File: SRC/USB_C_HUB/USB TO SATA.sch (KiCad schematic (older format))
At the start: 48 parts, among them J7 Bus_M.2_Socket_M, U9 TUSB9261, Y5 40MHz

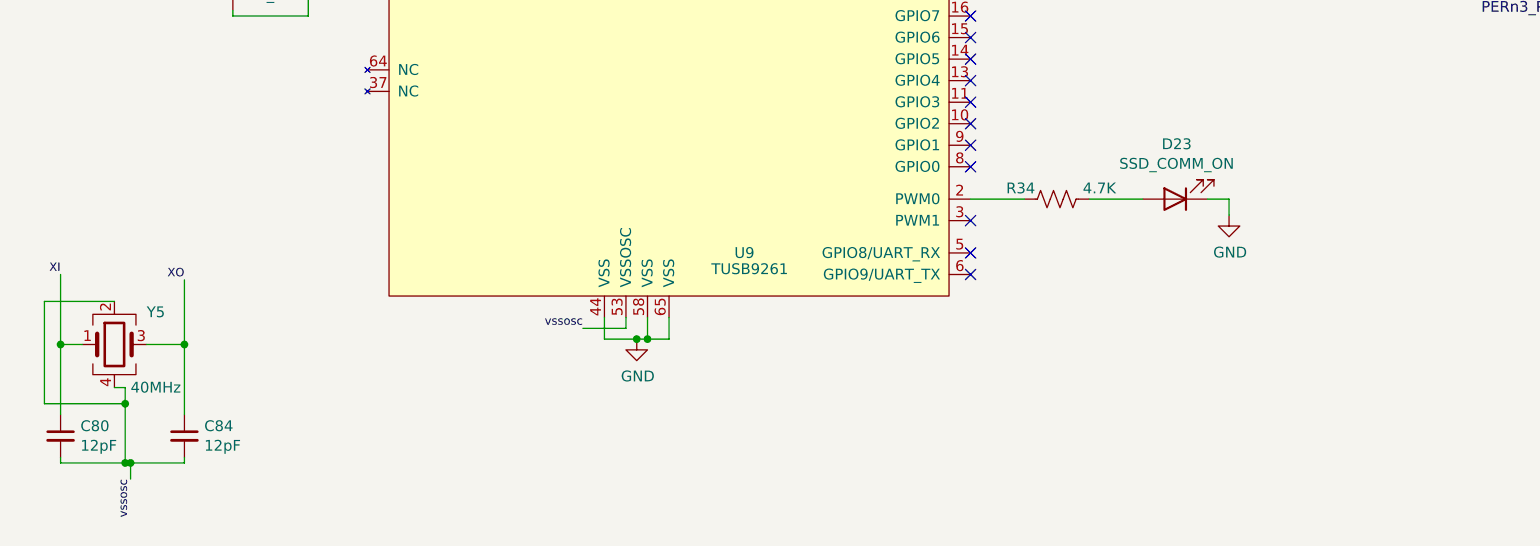
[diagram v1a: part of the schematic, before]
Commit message: schematic capture and footprint assignment complete. Pending approval
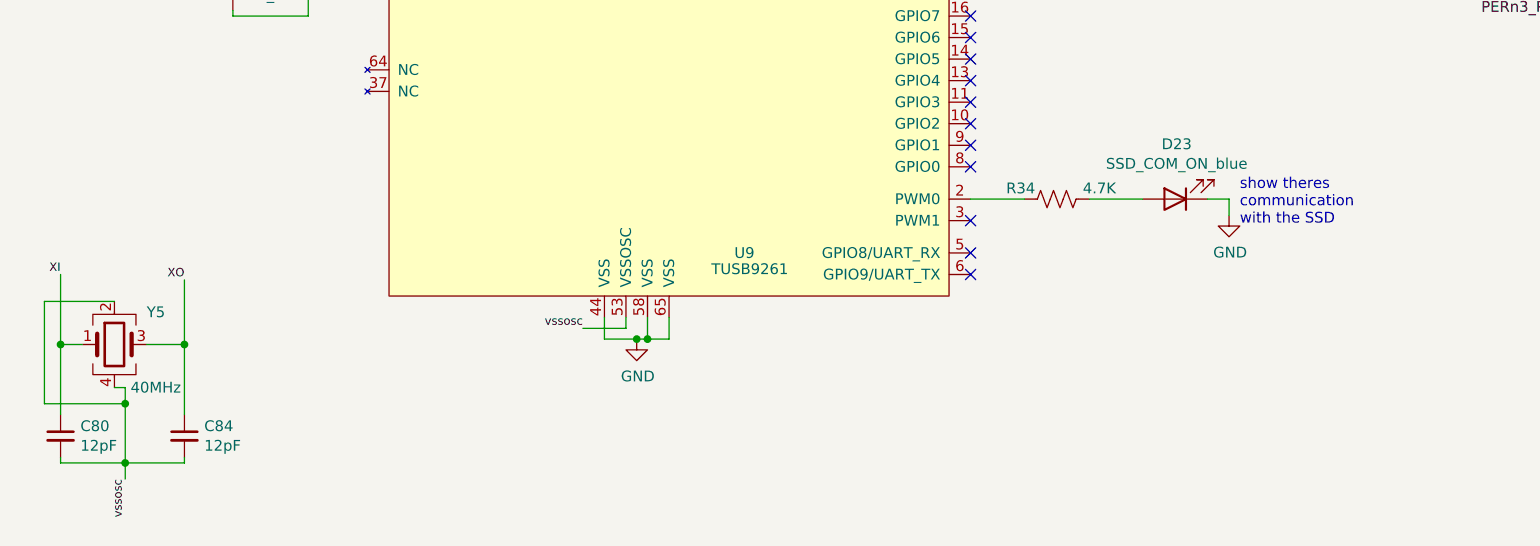
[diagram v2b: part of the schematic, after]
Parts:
- C100, C81: footprint (none) -> Capacitor_SMD:C_0402_1005Metric; Mfr No. (none) -> CL05A105KQ5NNNC
- C101: footprint (none) -> Capacitor_SMD:C_0402_1005Metric; Mfr No. (none) -> GRM155R60J226ME11D
- C102, C103, C104, C105, C106, C107, C108, C109, C110, C111, C112, C113, C114, C82, C83, C85, C86, C87, C88, C89, C90, C91, C92, C93, C94, C95, C96, C97, C98, C99: footprint (none) -> Capacitor_SMD:C_0402_1005Metric
- C79: footprint (none) -> Capacitor_SMD:C_0402_1005Metric; Mfr No. (none) -> C0402C103J5RECAUTO
- C80, C84: footprint (none) -> Capacitor_SMD:C_0402_1005Metric; Mfr No. (none) -> 0402CG120J500NT
- D23: value SSD_COMM_ON -> SSD_COM_ON_blue; footprint (none) -> LED_SMD:LED_0603_1608Metric; Field4 (none) -> 19-217/BHC-ZL1M2RY/3T
- J7: footprint (none) -> footprints:TE_1-2199119-3
- R101, R30, R31, R32, R33, R34, R35: footprint (none) -> Resistor_SMD:R_0402_1005Metric
- R29: footprint (none) -> Resistor_SMD:R_0402_1005Metric; Mfr No. (none) -> 0402WGF9092TCE
- U9: footprint (none) -> footprints:QFP40P900X900X120-65N
- Y5: footprint (none) -> Crystal:Crystal_SMD_2520-4Pin_2.5x2.0mm
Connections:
- wire segments 262 -> 261
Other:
- note added: "show theres \ncommunication \nwith the SSD"
